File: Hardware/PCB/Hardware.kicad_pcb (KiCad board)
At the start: 2 copper layers, 68.6 x 53.3 mm, 36 parts, among them J1 Conn_01x03_Male, M1 Motor_Servo, M2 Motor_Servo, M3 Motor_Servo, P1 Power, P2 Analog, P3 Digital, P4 Digital, P5 CONN_01X01, P6 CONN_01X01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

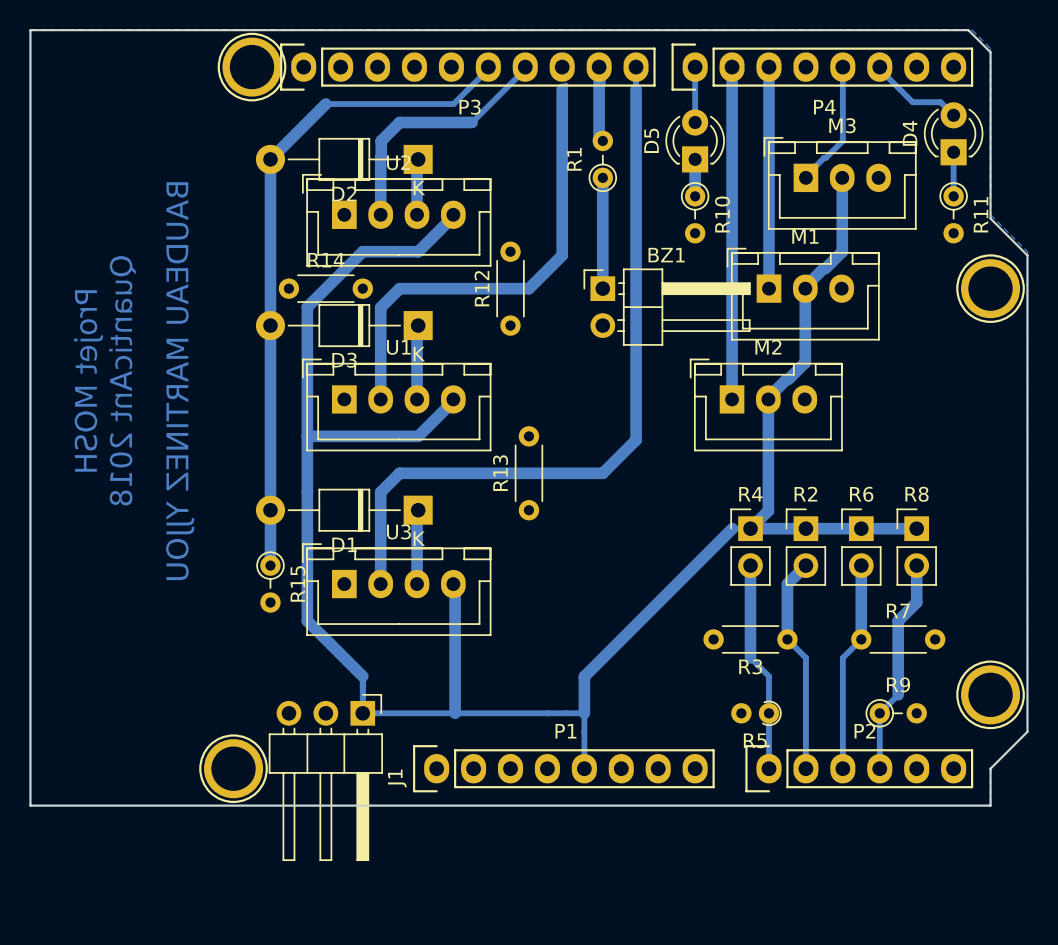
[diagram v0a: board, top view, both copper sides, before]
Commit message: Premieres modifs apres commentaire de cathy
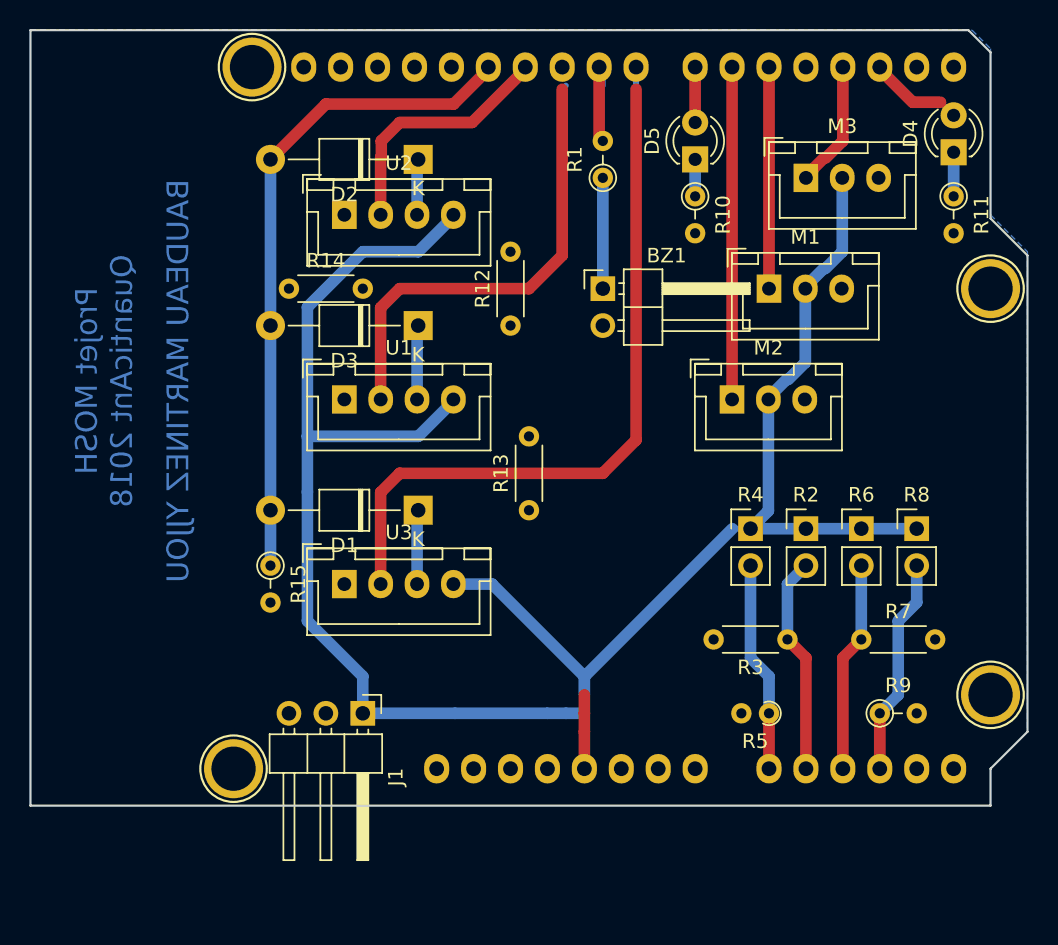
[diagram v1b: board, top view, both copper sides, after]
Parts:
- P1, P2, P3, P4: moved to B.Cu
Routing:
- net +5V: track 142.5 -> 146.8 mm

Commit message: PCB final
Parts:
- removed R12, R13, R14: R, Resistor_THT:R_Axial_DIN0204_L3.6mm_D1.6mm_P5.08mm_Horizontal
- added R17: R, Resistor_THT:R_Axial_DIN0207_L6.3mm_D2.5mm_P10.16mm_Horizontal, F.Cu at (142.7, 93.3)
- added R18: R, Resistor_THT:R_Axial_DIN0207_L6.3mm_D2.5mm_P10.16mm_Horizontal, F.Cu at (142.7, 80.6)
- added R19: R, Resistor_THT:R_Axial_DIN0207_L6.3mm_D2.5mm_P10.16mm_Horizontal, F.Cu at (142.7, 104.8)
- added R20: R, Resistor_THT:R_Axial_DIN0207_L6.3mm_D2.5mm_P10.16mm_Horizontal, F.Cu at (163.1, 79.4)
- added R21: R, Resistor_THT:R_Axial_DIN0207_L6.3mm_D2.5mm_P10.16mm_Horizontal, F.Cu at (159.3, 79.4)
- added R22: R, Resistor_THT:R_Axial_DIN0207_L6.3mm_D2.5mm_P10.16mm_Horizontal, F.Cu at (166.9, 79.4)
- BZ1: footprint Connector_PinHeader_2.54mm:PinHeader_1x02_P2.54mm_Horizontal -> Connector_PinHeader_2.54mm:PinHeader_1x02_P2.54mm_Vertical
- R1, R10, R11, R15, R9: footprint Resistor_THT:R_Axial_DIN0204_L3.6mm_D1.6mm_P2.54mm_Vertical -> Resistor_THT:R_Axial_DIN0207_L6.3mm_D2.5mm_P10.16mm_Horizontal
- R3, R7: footprint Resistor_THT:R_Axial_DIN0204_L3.6mm_D1.6mm_P5.08mm_Horizontal -> Resistor_THT:R_Axial_DIN0207_L6.3mm_D2.5mm_P10.16mm_Horizontal
- R5: footprint Resistor_THT:R_Axial_DIN0204_L3.6mm_D1.6mm_P1.90mm_Vertical -> Resistor_THT:R_Axial_DIN0207_L6.3mm_D2.5mm_P10.16mm_Horizontal
- moved R1 15.7 mm to (146.6, 98.4)
- moved M3 14.5 mm to (173.2, 94.6), turned to 270 degrees
- moved BZ1 12.0 mm to (146.6, 102.2)
- moved D1 11.7 mm to (126.2, 108.6), turned to 270 degrees
- moved D2 11.5 mm to (126.2, 80.6), turned to 270 degrees
- moved D3 11.5 mm to (126.2, 94.6), turned to 270 degrees
- moved R15 10.2 mm to (132.6, 118.7), turned to 0 degrees
- moved R5 7.73 mm to (163.1, 112.4)
- moved R9 7.73 mm to (168.1, 112.4)
- moved R11 6.35 mm to (170.7, 79.4)
- moved D5 6.35 mm to (151.6, 85.7)
- moved M1 5.39 mm to (165.6, 94.6), turned to 270 degrees
- moved R10 5.24 mm to (155.4, 79.4)
- moved D4 4.30 mm to (174.5, 85.7)
- moved M2 4.02 mm to (158.0, 94.6), turned to 270 degrees
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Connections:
- M1 pad 1: /5(**) -> Net-(M1-Pad1)
- M2 pad 1: /6(**) -> Net-(M2-Pad1)
- M3 pad 1: /3(**) -> Net-(M3-Pad1)
- P3 pad 1: /A5(SCL) -> Net-(P3-Pad1)
- P3 pad 2: /A4(SDA) -> Net-(P3-Pad2)
- U1 pad 2: /10(**/SS) -> Net-(R17-Pad2)
- U2 pad 2: /11(**/MOSI) -> Net-(R18-Pad2)
- U3 pad 2: /8 -> Net-(R19-Pad2)
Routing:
- net GND: track 0.00 -> 51.1 mm
- net +5V: track 146.8 -> 125.2 mm
- net /8: track 52.7 -> 33.3 mm
- net /12(MISO): track 45.6 -> 64.9 mm
- net /6(**): track 22.9 -> 3.81 mm
- net Net-(D1-Pad1): track 5.24 -> 21.2 mm
- net Net-(D2-Pad1): track 4.08 -> 18.1 mm
- net Net-(D3-Pad1): track 5.24 -> 18.5 mm
- net /10(**/SS): track 32.4 -> 19.9 mm
- net /5(**): track 15.2 -> 4.34 mm
- net /11(**/MOSI): track 17.4 -> 6.52 mm
- net Net-(M3-Pad1): track 0.00 -> 8.45 mm
- net /9(**): track 6.56 -> 14.8 mm
- net Net-(D5-Pad1): track 2.54 -> 8.92 mm
- net Net-(R18-Pad2): track 0.00 -> 6.30 mm
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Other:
- net class Default: trace_width 0.5 -> 0.8
- board text added: "**QuanticAnt** - Projet MOSH 2018 -"
- board text added: "BOTTOM"
- board text added: "TOP"
